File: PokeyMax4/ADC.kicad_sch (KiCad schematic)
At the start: 5 parts

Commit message: Update the v4 board
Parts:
- C12: JLCPCB Part # C452745 -> (none); LCSC Part # (none) -> C12530
- C7: JLCPCB Part # C93920 -> (none); LCSC Part # (none) -> C1523
- R10: JLCPCB Part # C102771 -> (none); LCSC Part # (none) -> C25860
- R8, R9: JLCPCB Part # C384338 -> (none); LCSC Part # (none) -> C25890

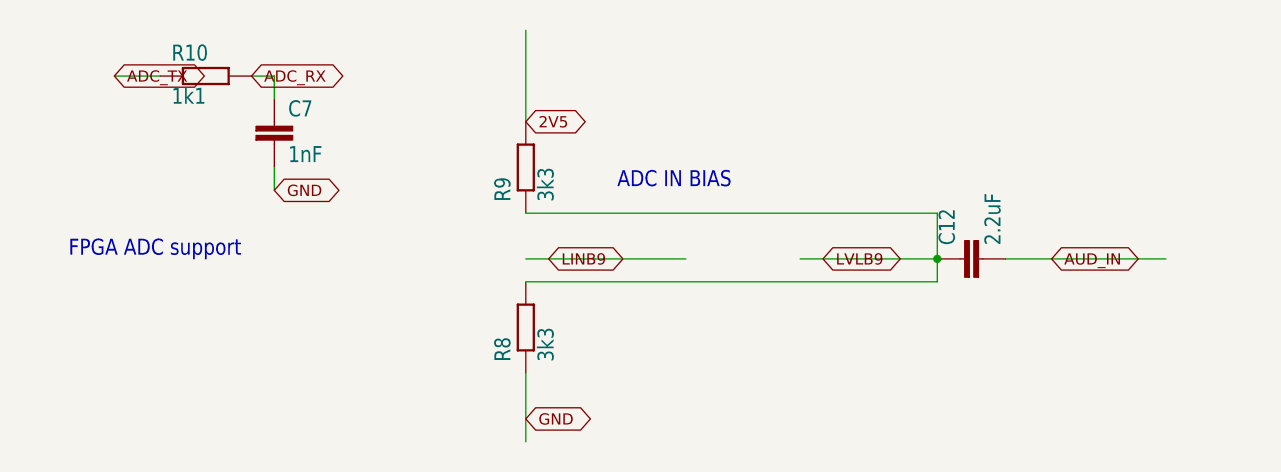
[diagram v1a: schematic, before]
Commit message: Updates for JLCPCB fabrication and parts library
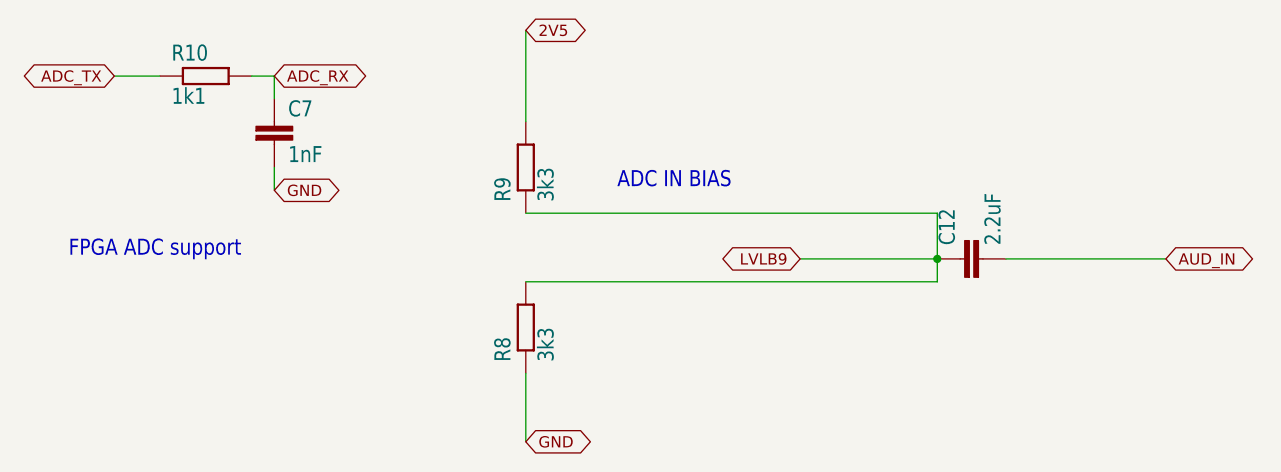
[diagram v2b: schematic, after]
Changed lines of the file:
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@@
 	(wire
 		(pts
-			(xy 137.16 106.68) (xy 154.94 106.68)
+			(xy 137.16 101.6) (xy 182.88 101.6)
 		)
 		(stroke
@@
 	(wire
 		(pts
-			(xy 137.16 101.6) (xy 182.88 101.6)
+			(xy 167.64 106.68) (xy 182.88 106.68)
 		)
 		(stroke
@@
 	(wire
 		(pts
-			(xy 167.64 106.68) (xy 182.88 106.68)
+			(xy 182.88 109.22) (xy 182.88 106.68)
 		)
 		(stroke
@@
 	(wire
 		(pts
-			(xy 182.88 109.22) (xy 182.88 106.68)
+			(xy 109.22 99.06) (xy 109.22 96.52)
 		)
 		(stroke
@@
 	(wire
 		(pts
-			(xy 109.22 99.06) (xy 109.22 96.52)
+			(xy 190.5 106.68) (xy 208.28 106.68)
 		)
 		(stroke
@@
 		)
 	)
-	(wire
-		(pts
-			(xy 190.5 106.68) (xy 208.28 106.68)
-		)
-		(stroke
-			(width 0.1524)
-			(type solid)
-		)
-	)
 	(text "ADC IN BIAS"
 		(exclude_from_sim no)
@@
 	(global_label "ADC_TX"
 		(shape bidirectional)
-		(at 91.44 86.36 0)
+		(at 91.44 86.36 180)
 		(fields_autoplaced yes)
 		(effects
@@
 				(size 1.2446 1.2446)
 			)
-			(justify left)
+			(justify right)
 		)
 		(property "Intersheetrefs" "${INTERSHEET_REFS}"
@@
 	(global_label "GND"
 		(shape bidirectional)
-		(at 137.16 124.46 0)
+		(at 137.16 127 0)
 		(fields_autoplaced yes)
 		(effects
@@
 		)
 		(property "Intersheetrefs" "${INTERSHEET_REFS}"
-			(at 144.9673 124.46 0)
-			(effects
-				(font
-					(size 1.27 1.27)
-				)
-				(justify left)
-				(hide yes)
-			)
-		)
-	)
-	(global_label "LINB9"
-		(shape bidirectional)
-		(at 139.7 106.68 0)
-		(fields_autoplaced yes)
-		(effects
-			(font
-				(size 1.2446 1.2446)
-			)
-			(justify left)
-		)
-		(property "Intersheetrefs" "${INTERSHEET_REFS}"
-			(at 149.0482 106.68 0)
+			(at 144.9673 127 0)
 			(effects
 				(font
@@
 	(global_label "2V5"
 		(shape bidirectional)
-		(at 137.16 91.44 0)
+		(at 137.16 81.28 0)
 		(fields_autoplaced yes)
 		(effects
@@
 		)
 		(property "Intersheetrefs" "${INTERSHEET_REFS}"
-			(at 144.6116 91.44 0)
+			(at 144.6116 81.28 0)
 			(effects
 				(font
@@
 	(global_label "AUD_IN"
 		(shape bidirectional)
-		(at 195.58 106.68 0)
+		(at 208.28 106.68 0)
 		(fields_autoplaced yes)
 		(effects
@@
 		)
 		(property "Intersheetrefs" "${INTERSHEET_REFS}"
-			(at 206.0544 106.68 0)
+			(at 218.7544 106.68 0)
 			(effects
 				(font
@@
 	(global_label "ADC_RX"
 		(shape bidirectional)
-		(at 106.68 86.36 0)
+		(at 109.22 86.36 0)
 		(fields_autoplaced yes)
 		(effects
@@
 		)
 		(property "Intersheetrefs" "${INTERSHEET_REFS}"
-			(at 117.6284 86.36 0)
+			(at 120.1684 86.36 0)
 			(effects
 				(font
@@
 	(global_label "LVLB9"
 		(shape bidirectional)
-		(at 170.18 106.68 0)
+		(at 167.64 106.68 180)
 		(fields_autoplaced yes)
 		(effects
@@
 				(size 1.2446 1.2446)
 			)
-			(justify left)
+			(justify right)
 		)
 		(property "Intersheetrefs" "${INTERSHEET_REFS}"
-			(at 179.7059 106.68 0)
+			(at 177.1659 106.68 0)
 			(effects
 				(font
@@
 			)
 		)
+		(property "JLCPCB Rotation Offset" ""
+			(at 185.42 106.68 0)
+			(effects
+				(font
+					(size 1.27 1.27)
+				)
+				(hide yes)
+			)
+		)
 		(pin "2"
 		)
@@
 			)
 		)
+		(property "JLCPCB Rotation Offset" ""
+			(at 109.22 91.44 0)
+			(effects
+				(font
+					(size 1.27 1.27)
+				)
+				(hide yes)
+			)
+		)
 		(pin "1"
 		)
@@
 			)
 		)
+		(property "JLCPCB Rotation Offset" ""
+			(at 137.16 114.3 0)
+			(effects
+				(font
+					(size 1.27 1.27)
+				)
+				(hide yes)
+			)
+		)
 		(pin "2"
 		)
@@
 			)
 		)
+		(property "JLCPCB Rotation Offset" ""
+			(at 137.16 96.52 0)
+			(effects
+				(font
+					(size 1.27 1.27)
+				)
+				(hide yes)
+			)
+		)
 		(pin "1"
 		)
@@
 			(at 101.6 86.36 0)
 			(effects
+				(font
+					(size 1.27 1.27)
+				)
+				(hide yes)
+			)
+		)
+		(property "JLCPCB Rotation Offset" ""
+			(at 101.6 86.36 0)
+			(effects

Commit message: Update BOM from 0402 to 0603 where relevant
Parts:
- C12: LCSC Part # C12530 -> C43922
- C7: LCSC Part # C1523 -> C1636
- R10: LCSC Part # C25860 -> C140120
- R8, R9: LCSC Part # C25890 -> C72816
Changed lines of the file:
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@@
 			)
 		)
-		(property "LCSC Part #" "C12530"
+		(property "LCSC Part #" "C43922"
 			(at 185.42 106.68 0)
 			(effects
@@
 			)
 		)
-		(property "LCSC Part #" " C1523"
+		(property "LCSC Part #" "C1636"
 			(at 109.22 91.44 0)
 			(effects
@@
 			)
 		)
-		(property "LCSC Part #" "C25890"
+		(property "LCSC Part #" "C72816"
 			(at 137.16 114.3 0)
 			(effects
@@
 			)
 		)
-		(property "LCSC Part #" "C25890"
+		(property "LCSC Part #" "C72816"
 			(at 137.16 96.52 0)
 			(effects
@@
 			)
 		)
-		(property "LCSC Part #" "C25860"
+		(property "LCSC Part #" "C140120"
 			(at 101.6 86.36 0)
 			(effects
